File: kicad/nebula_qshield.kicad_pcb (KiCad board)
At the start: 4 copper layers, 100 x 120 mm, 162 parts, among them J1 J1, J10 J10, J11 J11, J12 J12, J13 J13, J14 J14, J15 J15, J16 J16, J17 J17, J18 J18, J19 J19, J2 J2, J20 J20, J21 Arduino UNO Q Shield, J3 J3, J4 J4, J5 J5, J6 J6, J7 J7, J8 J8, J9 J9, K1 HF46F-12-HS1, K2 HF46F-12-HS1, Q1 IRLZ44NPBF, Q2 IRLZ44NPBF, Q3 2N7002, Q4 2N7002, Q5 IRLZ44NPBF, SW1 RESET, T1 Transformer_SP_2S, T2 Transformer_SP_2S, T3 Transformer_SP_2S, U1 TPS54302DDCR, U10 MCP6002, U11 MCP6002, U12 SN6501, U13 AMC1301, U14 HX711, U15 MAX485ESA, U16 PC817X2NIP, U17 IR2104SPBF, U18 PC817X1NIP, U19 PC817X1NIP, U2 AMS1117-3.3, U20 MCP6002, U21 ISO1541, U22 SC16IS740, U23 SN74LVC1G04, U3 TPS3823-33DBVR, U4 MCP6002, U5 SN6501, U6 AMC1301, U7 MCP6002, U8 SN6501, U9 AMC1301, Y1 1.8432MHz

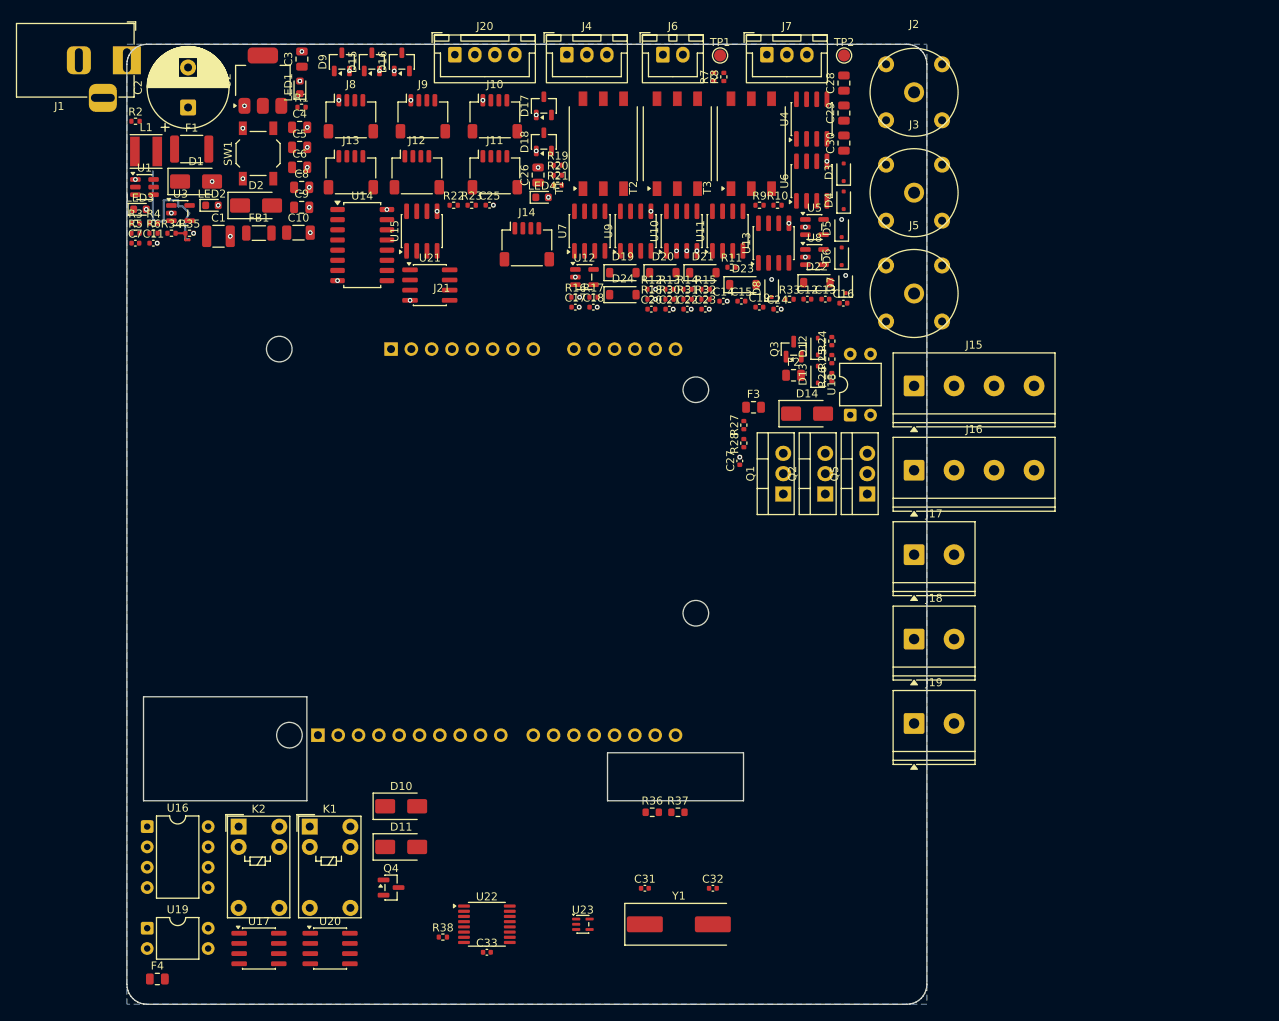
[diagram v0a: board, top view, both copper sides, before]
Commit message: feat(pcb): Fase 4 power routing baseline
- Add 2 M3 case mounting holes (H1, H2) in DRC-clean positions.
- Import FreeRouting pass; manually fix /12V_RAIL route near C1 to
  clear C1 GND pad and MCU_NRST net.
- Adjust /I2C_SDA trace near cutout to meet copper edge clearance.
- DRC severity-error: 0 violations, 115 unconnected items remaining.
- ERC: 0 violations.

Co-Authored-By: Devin AI <158243242+devin-ai-integration[bot]@users.noreply.github.com>
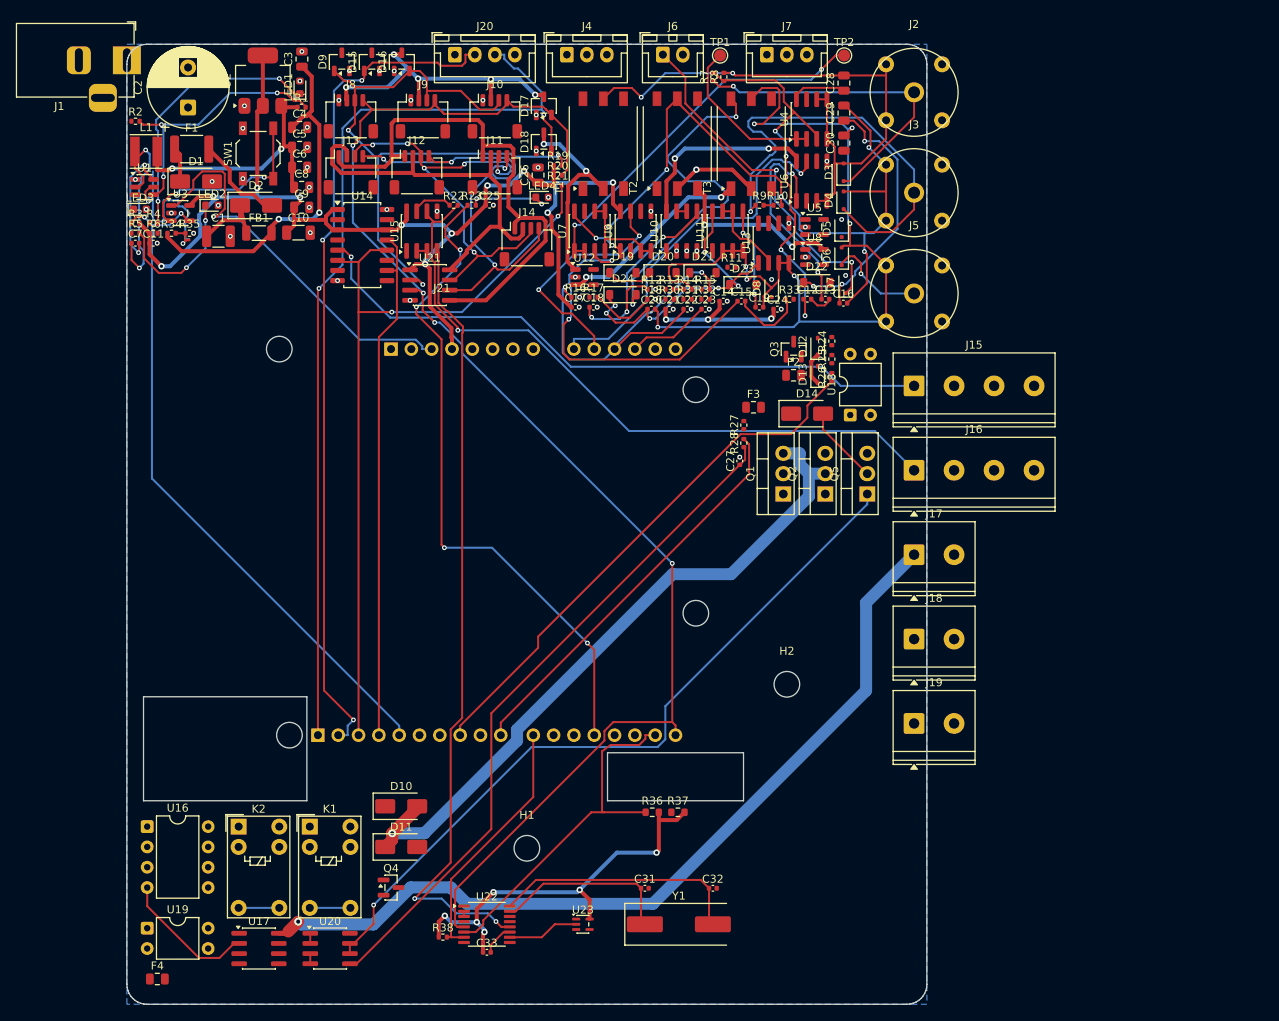
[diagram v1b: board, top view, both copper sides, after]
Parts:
- added H1: MountingHole_3.2mm_M3, MountingHole_3.2mm_M3, F.Cu at (50.0, 100.5)
- added H2: MountingHole_3.2mm_M3, MountingHole_3.2mm_M3, F.Cu at (82.5, 80.0)
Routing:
- net /3V3_RAIL: track 0.00 -> 286.1 mm, vias 0 -> 27
- net /I2C_SCL: track 0.00 -> 175.8 mm, vias 0 -> 4
- net /I2C_SDA: track 0.00 -> 127.0 mm, vias 0 -> 3
- net /Analog Acquisition/GND_ISO_DO: track 0.00 -> 122.2 mm, vias 0 -> 7
- net /HMI & Connectors/HMI_RX: track 0.00 -> 118.9 mm, vias 0 -> 2
- net /Analog Acquisition/GND_ISO_ORP: track 0.00 -> 111.5 mm, vias 0 -> 5
- net /Actuator Drivers/MOTOR_VB: track 0.00 -> 107.4 mm, vias 0 -> 1
- net /HMI & Connectors/HMI_TX: track 0.00 -> 105.1 mm, vias 0 -> 3
- net /HX711_DOUT: track 0.00 -> 100.0 mm, vias 0 -> 2
- net /Digital & I2C/RS485_DI: track 0.00 -> 98.2 mm, vias 0 -> 2
- net /Actuator Drivers/CO2_PWM_OUT: track 0.00 -> 93.8 mm, vias 0 -> 1
- net /Actuator Drivers/MOTOR_VS: track 0.00 -> 87.0 mm, vias 0 -> 1
- net /MCU_WDI: track 0.00 -> 85.6 mm, vias 0 -> 2
- net /Actuator Drivers/CO2_PWM_FILT: track 0.00 -> 85.6 mm
- net /Digital & I2C/RS485_A: track 0.00 -> 84.8 mm, vias 0 -> 1
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
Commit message: feat(pcb): Fase 5 signal routing - 48 unconnected, DRC/ERC clean
Co-Authored-By: Devin AI <158243242+devin-ai-integration[bot]@users.noreply.github.com>
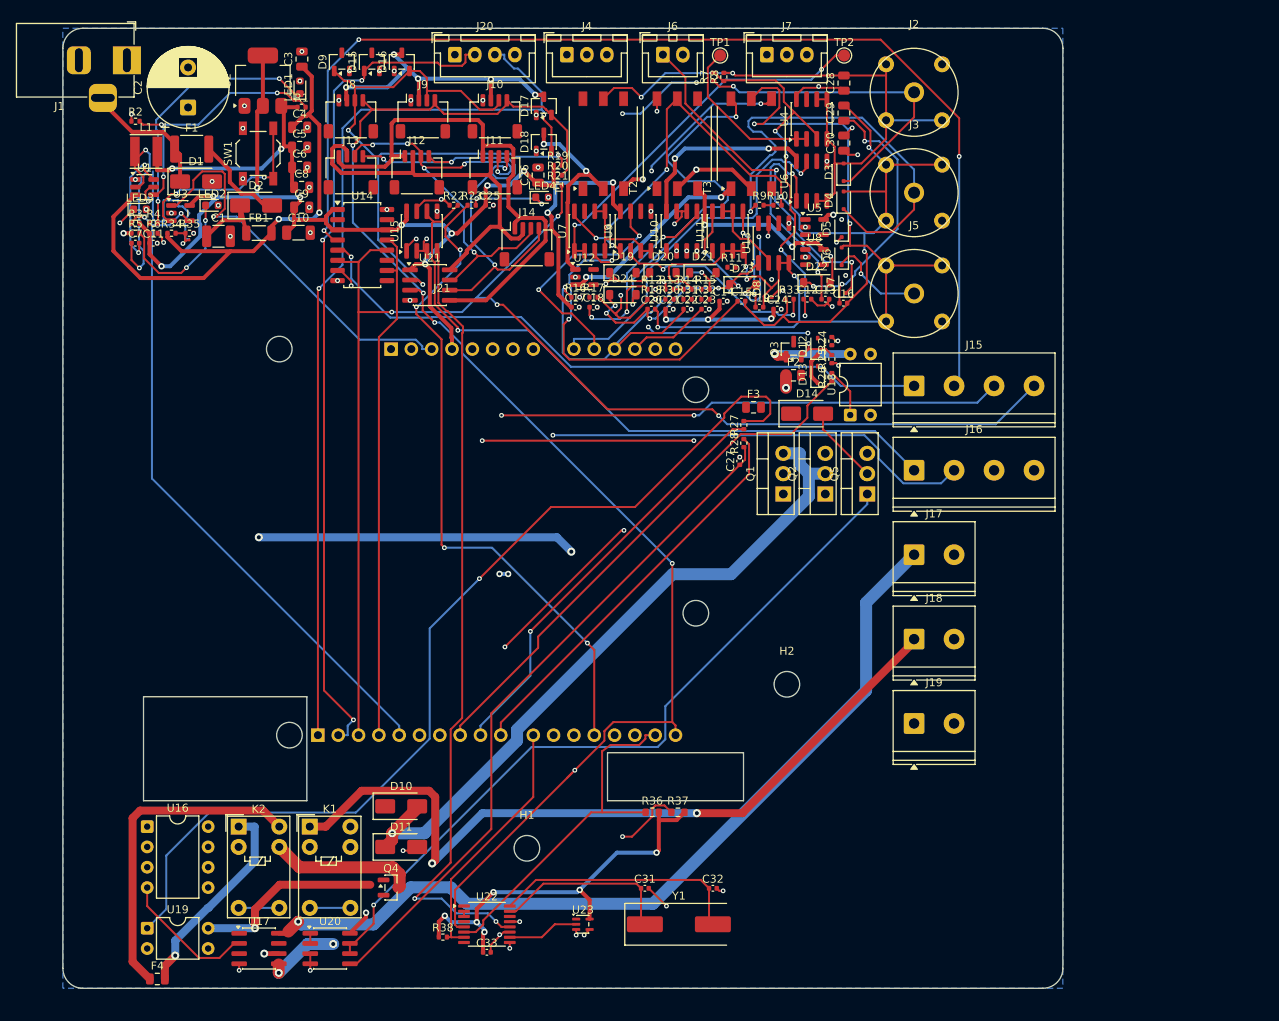
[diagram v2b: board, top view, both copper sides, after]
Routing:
- net /Actuator Drivers/CHILLER_OUT: track 0.00 -> 208.8 mm, vias 0 -> 3
- net /Digital & I2C/HX711_EN: track 0.00 -> 140.7 mm, vias 0 -> 3
- net /Actuator Drivers/U16_INA: track 0.00 -> 126.3 mm, vias 0 -> 3
- net /Actuator Drivers/U19_IN: track 0.00 -> 123.2 mm, vias 0 -> 1
- net /Actuator Drivers/MOTOR_LO: track 0.00 -> 113.2 mm, vias 0 -> 2
- net /Digital & I2C/RS485_DE: track 1.27 -> 99.9 mm, vias 0 -> 2
- net /Actuator Drivers/CO2_SOL_OUT: track 0.00 -> 98.4 mm, vias 0 -> 2
- net /5V_RAIL: track 69.1 -> 166.4 mm, vias 5 -> 9
- net /Digital & I2C/RS485_RO: track 0.00 -> 95.4 mm, vias 0 -> 2
- net /Digital & I2C/HX711_SP: track 0.00 -> 92.2 mm, vias 0 -> 3
- net /Digital & I2C/RS485_B: track 5.14 -> 94.9 mm, vias 0 -> 2
- net /HX711_DOUT: track 100.0 -> 178.2 mm, vias 2 -> 4
- net /I2C_SDA: track 127.0 -> 205.0 mm
- net /PUMP_PWM: track 0.00 -> 73.2 mm, vias 0 -> 3
- net /Analog Acquisition/VDD_ISO_PH: track 38.9 -> 100.9 mm, vias 2 -> 6
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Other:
- board size 100 x 120 mm -> 125 x 120 mm

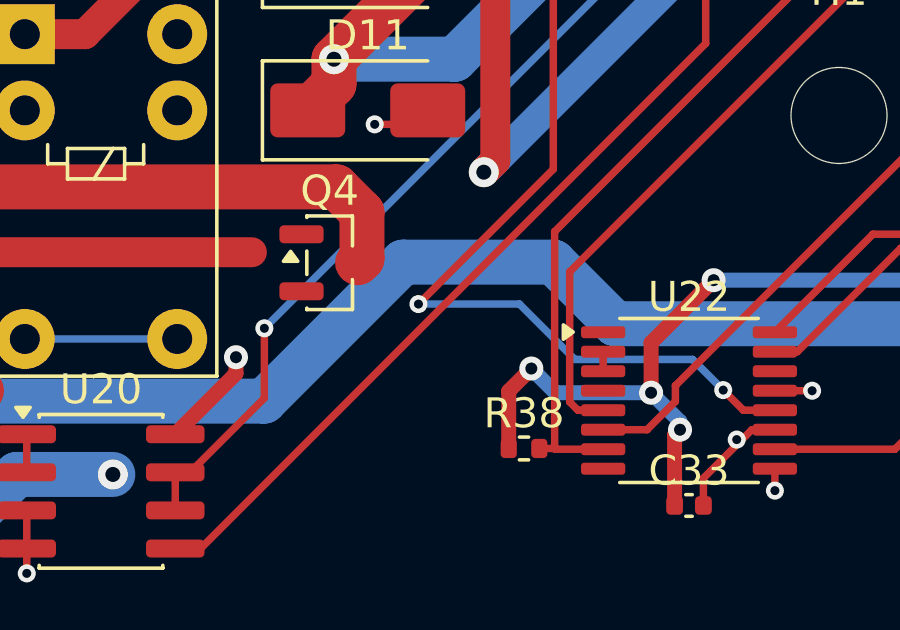
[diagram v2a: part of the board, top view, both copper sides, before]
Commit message: feat(pcb): Fase 5 continuation - FreeRouting pass reduces unconnected to 47, DRC/ERC clean
Co-Authored-By: Devin AI <158243242+devin-ai-integration[bot]@users.noreply.github.com>
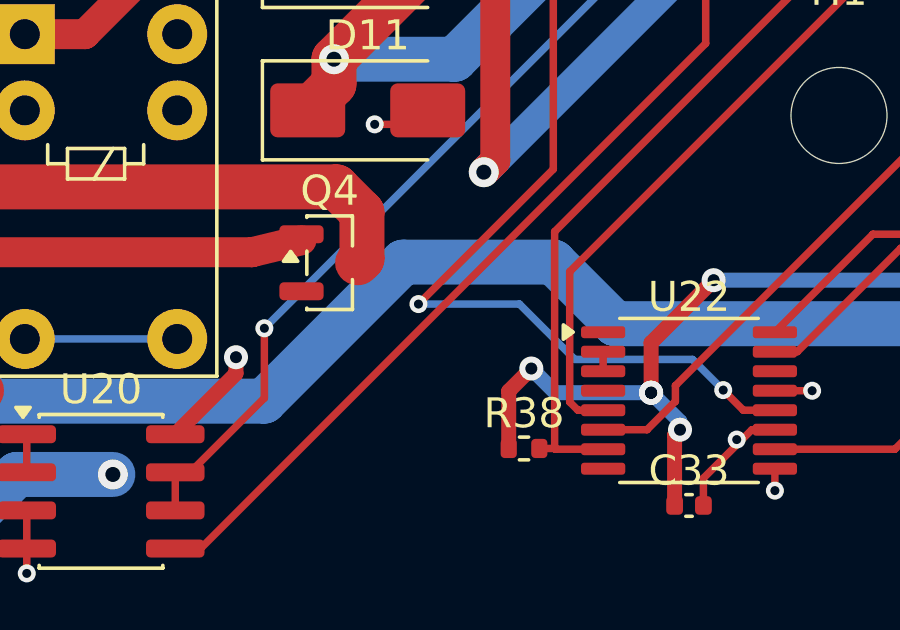
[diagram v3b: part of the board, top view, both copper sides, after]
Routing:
- net /Actuator Drivers/CHILLER_ISO: track 23.9 -> 25.6 mm
- net /3V3_RAIL: vias 27 -> 28

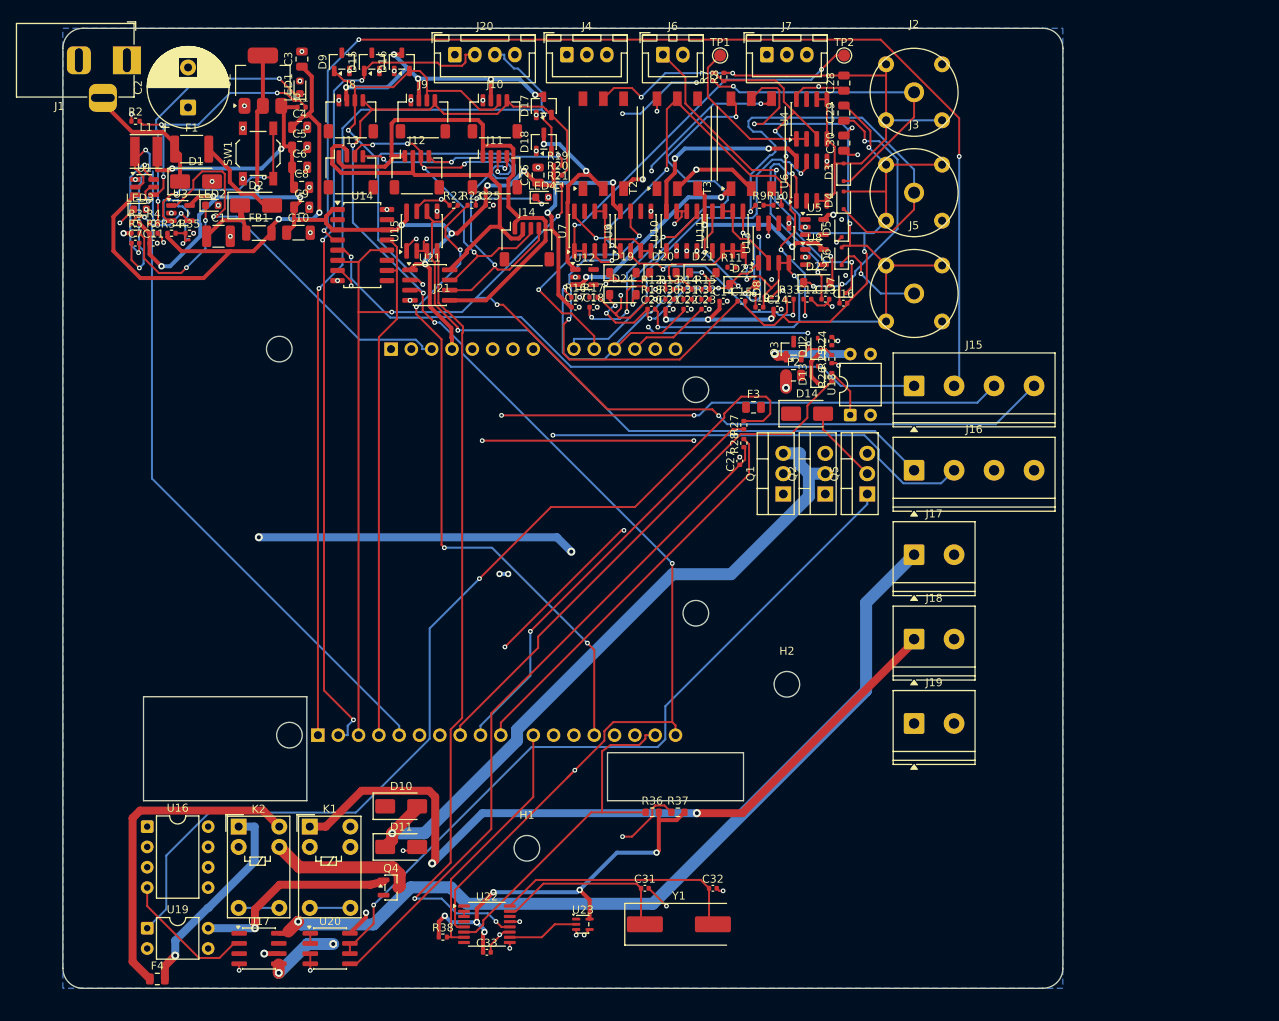
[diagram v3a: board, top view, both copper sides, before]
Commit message: feat(pcb): re-arquitectura 150x120 con placement Spark legalizado + FreeRouting, DRC 0, 86 unconnected
Co-Authored-By: Devin AI <158243242+devin-ai-integration[bot]@users.noreply.github.com>
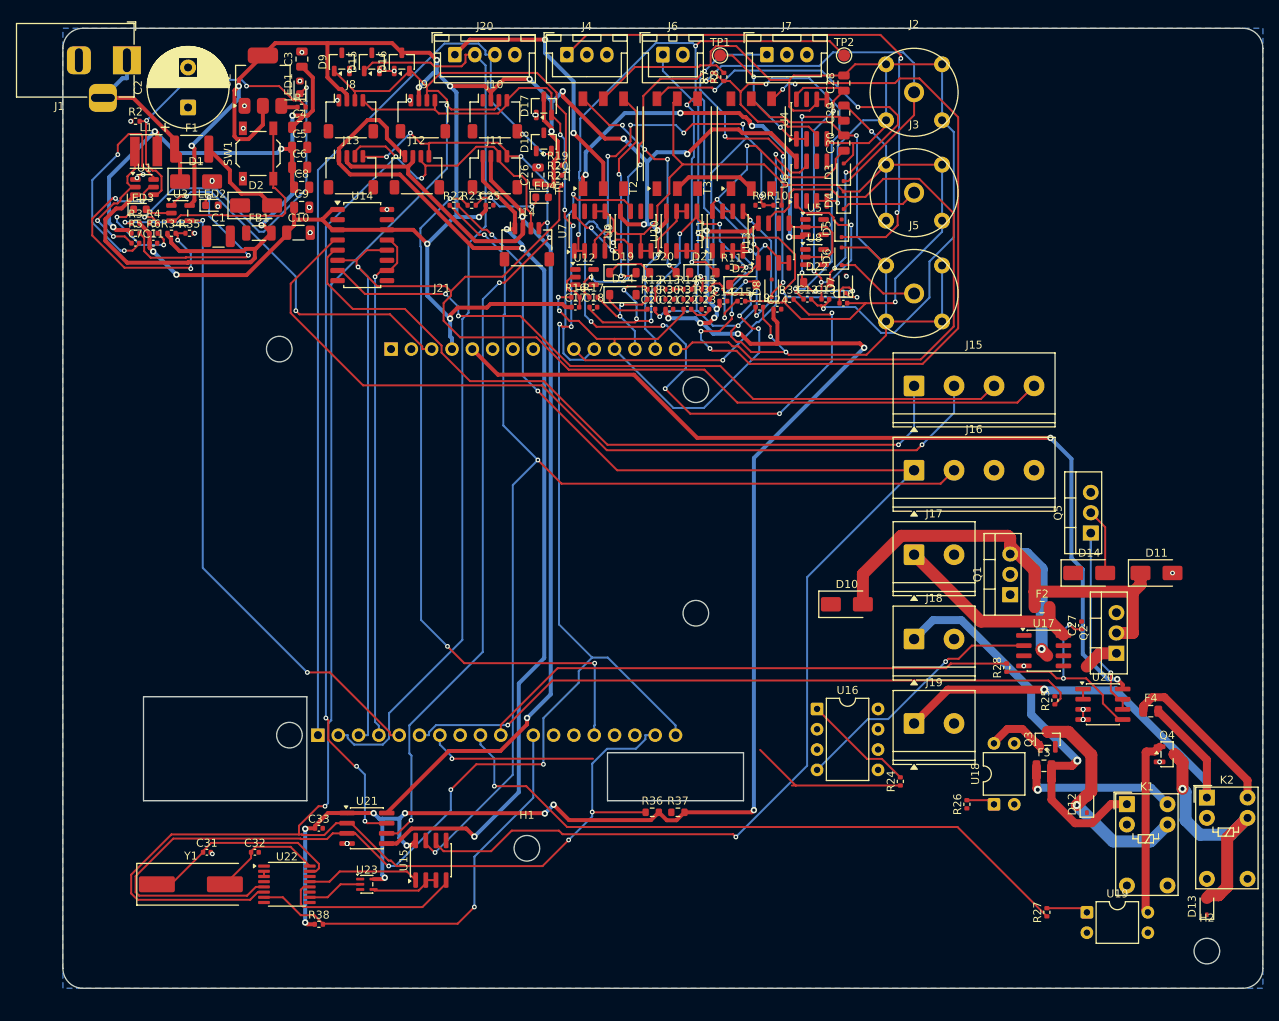
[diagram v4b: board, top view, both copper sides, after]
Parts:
- moved F4 128.6 mm to (128.0, 83.4)
- moved K2 121.1 mm to (135.0, 94.2)
- moved U19 117.5 mm to (120.0, 108.5)
- moved U17 104.9 mm to (114.6, 75.8)
- moved K1 102.2 mm to (125.0, 95.0)
- moved U20 101.3 mm to (122.0, 82.5)
- moved D11 100.4 mm to (128.7, 66.1)
- moved Q4 98.4 mm to (130.0, 88.8)
- moved U16 85.0 mm to (86.3, 83.1)
- moved D13 82.4 mm to (135.0, 107.8)
- moved U15 78.7 mm to (38.0, 102.0)
- moved R27 71.7 mm to (115.0, 108.5)
- moved U21 68.4 mm to (30.0, 98.0)
- moved D12 66.4 mm to (120.0, 95.0)
- moved H2 62.2 mm to (135.0, 113.4)
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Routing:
- net /3V3_RAIL: track 286.1 -> 475.5 mm, vias 28 -> 33
- net /Actuator Drivers/CHILLER_OUT: track 208.8 -> 58.4 mm, vias 3 -> 1
- net /Actuator Drivers/U19_IN: track 123.2 -> 5.58 mm, vias 1 -> 0
- net /Actuator Drivers/U16_INA: track 126.3 -> 14.0 mm, vias 3 -> 0
- net /Actuator Drivers/MOTOR_LO: track 113.2 -> 4.40 mm, vias 2 -> 0
- net /Digital & I2C/RS485_DE: track 99.9 -> 8.64 mm, vias 2 -> 0
- net /Digital & I2C/RS485_A: track 84.8 -> 173.6 mm, vias 1 -> 3
- net /Actuator Drivers/MOTOR_VB: track 107.4 -> 24.7 mm, vias 1 -> 0
- net /Digital & I2C/RS485_RO: track 95.4 -> 14.2 mm, vias 2 -> 0
- net /Digital & I2C/GND_ISO: track 65.8 -> 146.9 mm, vias 0 -> 3
- net /Digital & I2C/3V3_ISO: track 49.7 -> 128.9 mm, vias 0 -> 2
- net /Digital & I2C/RS485_DI: track 98.2 -> 23.0 mm, vias 2 -> 0
- net /Digital & I2C/SDA_ISO: track 54.7 -> 127.9 mm, vias 6 -> 5
- net /Actuator Drivers/CO2_PWM_OUT: track 93.8 -> 26.0 mm
- net /CO2_SOL_CTL: track 67.2 -> 0.00 mm
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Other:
- board size 125 x 120 mm -> 150 x 120 mm
